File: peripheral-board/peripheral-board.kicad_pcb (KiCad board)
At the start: 2 copper layers, 165 x 100 mm, 145 parts, among them CON1001 AVR-ISP-10, IC1001 ATTINY48-A, P1001 Peripheral Bus, P1002 Power, SW2001 1, SW2002 2, SW2003 3, SW2004 4, SW2005 5, SW2006 6, SW2007 7, SW2008 8, SW2009 9, SW2010 0, SW2011 +, SW2012 ´, SW2013 BKSP, SW2014 TROLL, SW2015 §, SW2016 UP, SW2017 RMB, SW2018 Q, SW2019 W, SW2020 E, SW2021 R, SW2022 T, SW2023 Y, SW2024 U, SW2025 I, SW2026 O, SW2027 P, SW2028 Å, SW2029 ¨, SW2030 RETURN, SW2031 ALT_GR, SW2032 <, SW2033 LEFT, SW2034 MMB, SW2035 A, SW2036 S, SW2037 D, SW2038 F, SW2039 G, SW2040 H, SW2041 J, SW2042 K, SW2043 L, SW2044 Ö, SW2045 Ä, SW2046 ', SW2047 ESC, SW2048 TAB, SW2049 ALT, SW2050 DOWN, SW2051 LMB, SW2052 SHIFT_L, SW2053 Z, SW2054 X, SW2055 C, SW2056 V, SW2057 B, SW2058 N, SW2059 M, SW2060 ,, SW2061 ., SW2062 -, SW2063 SHIFT_R, SW2064 FN_R, SW2065 SPACE, SW2066 FN_L, SW2067 RIGHT, SW2068 CTRL, U2001 4017, U2002 4017, U2003 74HC00, U6001 TCA0372

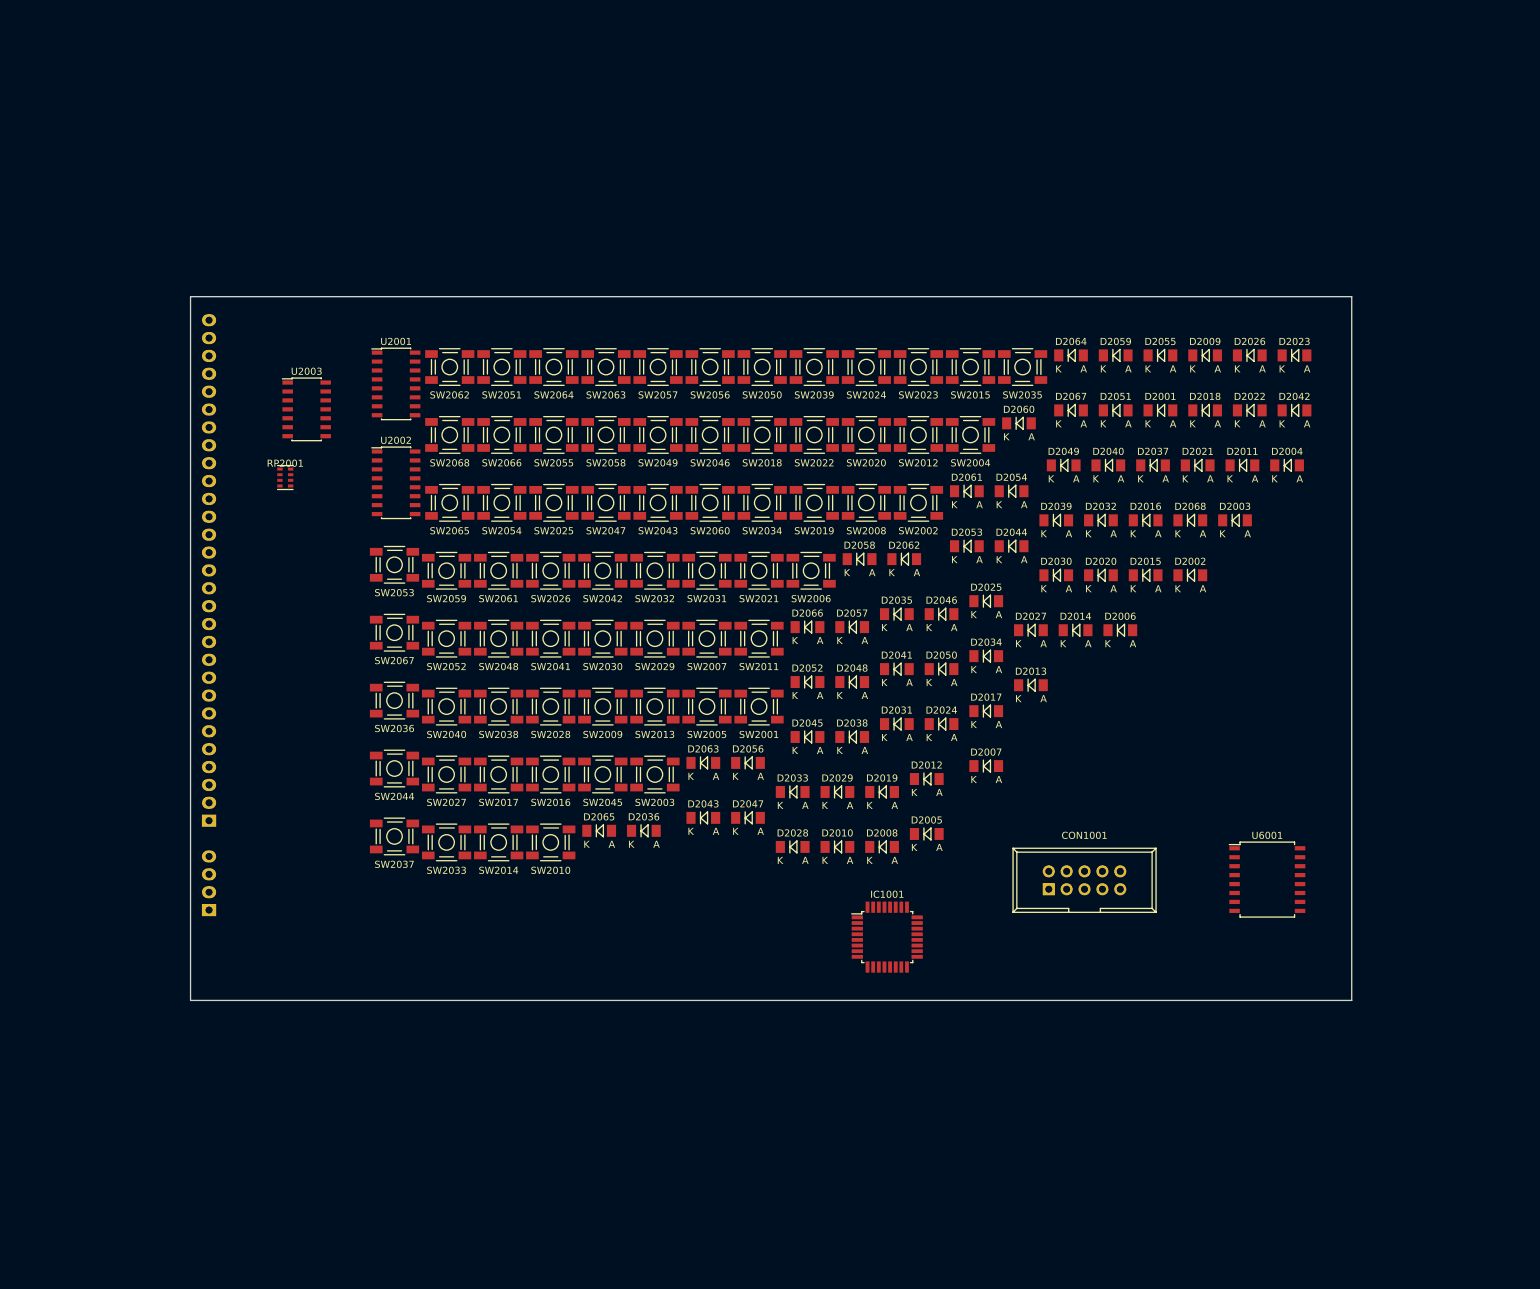
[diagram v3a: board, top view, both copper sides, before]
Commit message: keyboard switches and diodes placed
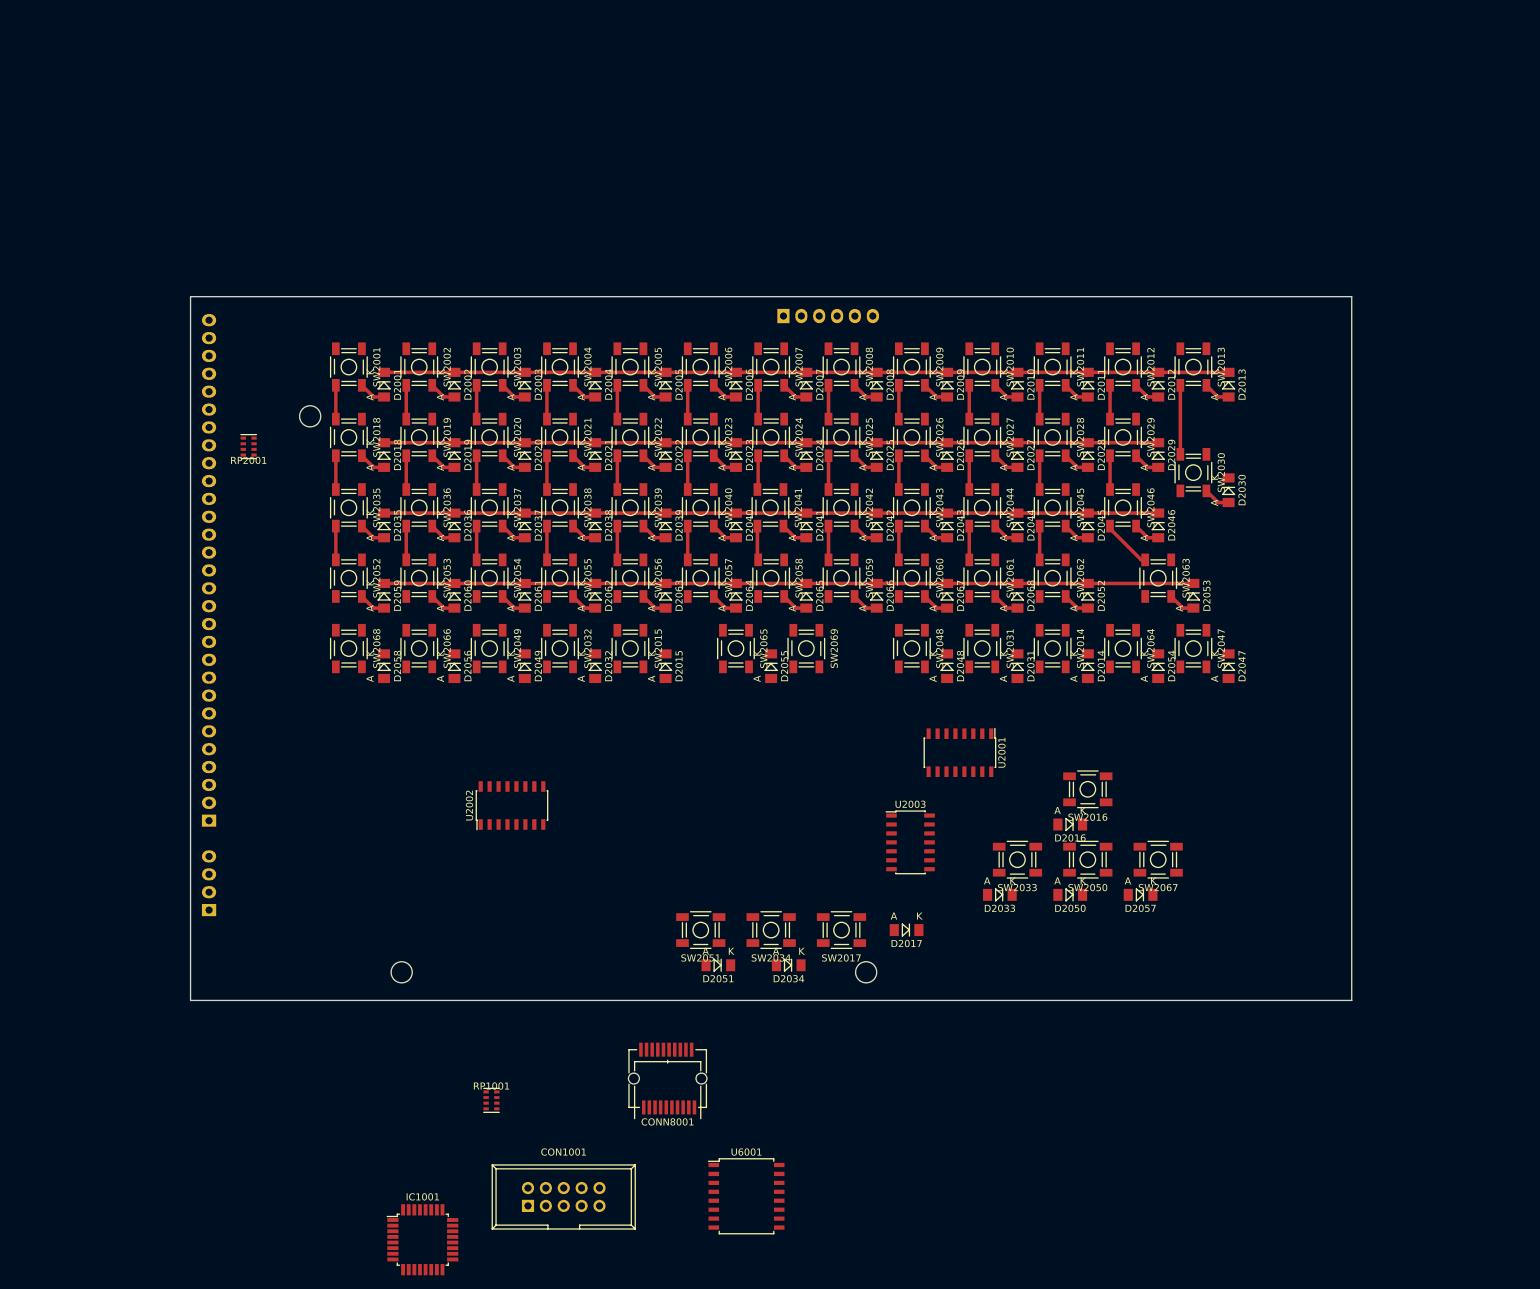
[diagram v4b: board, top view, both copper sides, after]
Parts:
- added CONN8001: 10056847-XY1LF, lib:10056847-XY1LF, F.Cu at (152.8, 161.1)
- added P9001: VGA, Socket_Strips:Socket_Strip_Straight_1x06, B.Cu at (169.2, 52.8)
- added REF**: 3mm, Mounting_Holes:MountingHole_3mm, F.Cu at (102.0, 67.0)
- added REF**: 3mm, Mounting_Holes:MountingHole_3mm, F.Cu at (181.0, 146.0)
- added REF**: 3mm, Mounting_Holes:MountingHole_3mm, F.Cu at (115.0, 146.0)
- added RP1001: 10k, Resistors_SMD:R_Cat16-4, F.Cu at (127.8, 164.2)
- added SW2069: SPACE, lib:SMD-TACT-5.2x5.2x2mm, F.Cu at (172.5, 100.0)
- moved D2018 116.8 mm to (112.5, 72.5), turned to 270 degrees
- moved SW2067 113.2 mm to (222.5, 130.0)
- moved D2001 110.4 mm to (112.5, 62.5), turned to 270 degrees
- moved D2059 109.4 mm to (112.5, 92.5), turned to 270 degrees
- moved D2002 108.0 mm to (122.5, 62.5), turned to 270 degrees
- moved U2003 105.6 mm to (187.3, 127.5)
- moved D2003 102.7 mm to (132.5, 62.5), turned to 270 degrees
- moved D2004 99.0 mm to (142.5, 62.5), turned to 270 degrees
- moved SW2035 97.8 mm to (107.5, 80.0), turned to 90 degrees
- moved D2051 97.0 mm to (160.0, 145.0), turned to 180 degrees
- moved U2001 95.7 mm to (194.3, 114.8), turned to 270 degrees
- moved SW2044 91.4 mm to (197.5, 80.0), turned to 90 degrees
- moved SW2010 91.2 mm to (197.5, 60.0), turned to 90 degrees
- moved SW2062 90.8 mm to (207.5, 90.0), turned to 90 degrees
- moved SW2013 90.5 mm to (227.5, 60.0), turned to 90 degrees
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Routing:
- net /Keyboard/Q0: track 0.00 -> 120.0 mm
- net /Keyboard/Q3: track 0.00 -> 115.0 mm
- net /Keyboard/Q2: track 0.00 -> 110.0 mm
- net /Keyboard/Q1: track 0.00 -> 110.0 mm
- net Net-(SW2012-Pad1): track 0.00 -> 16.8 mm
- net Net-(SW2007-Pad1): track 0.00 -> 14.5 mm
- net Net-(SW2011-Pad1): track 0.00 -> 14.4 mm
- net Net-(SW2010-Pad1): track 0.00 -> 14.4 mm
- net Net-(SW2009-Pad1): track 0.00 -> 14.4 mm
- net Net-(SW2008-Pad1): track 0.00 -> 14.4 mm
- net Net-(SW2006-Pad1): track 0.00 -> 14.4 mm
- net Net-(SW2005-Pad1): track 0.00 -> 14.4 mm
- net Net-(SW2004-Pad1): track 0.00 -> 14.4 mm
- net Net-(SW2003-Pad1): track 0.00 -> 14.4 mm
- net Net-(SW2002-Pad1): track 0.00 -> 14.4 mm
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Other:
- net class Default: clearance 0.2 -> 0.25; trace_width 0.25 -> 0.5; via_dia 0.8 -> 1; via_drill 0.4 -> 0.6
- rule trace_clearance: 0.2 -> 0.25
- rule via_min_drill: 0.3 -> 0.6
- rule via_min_size: 0.4 -> 1

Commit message: routed keyboard
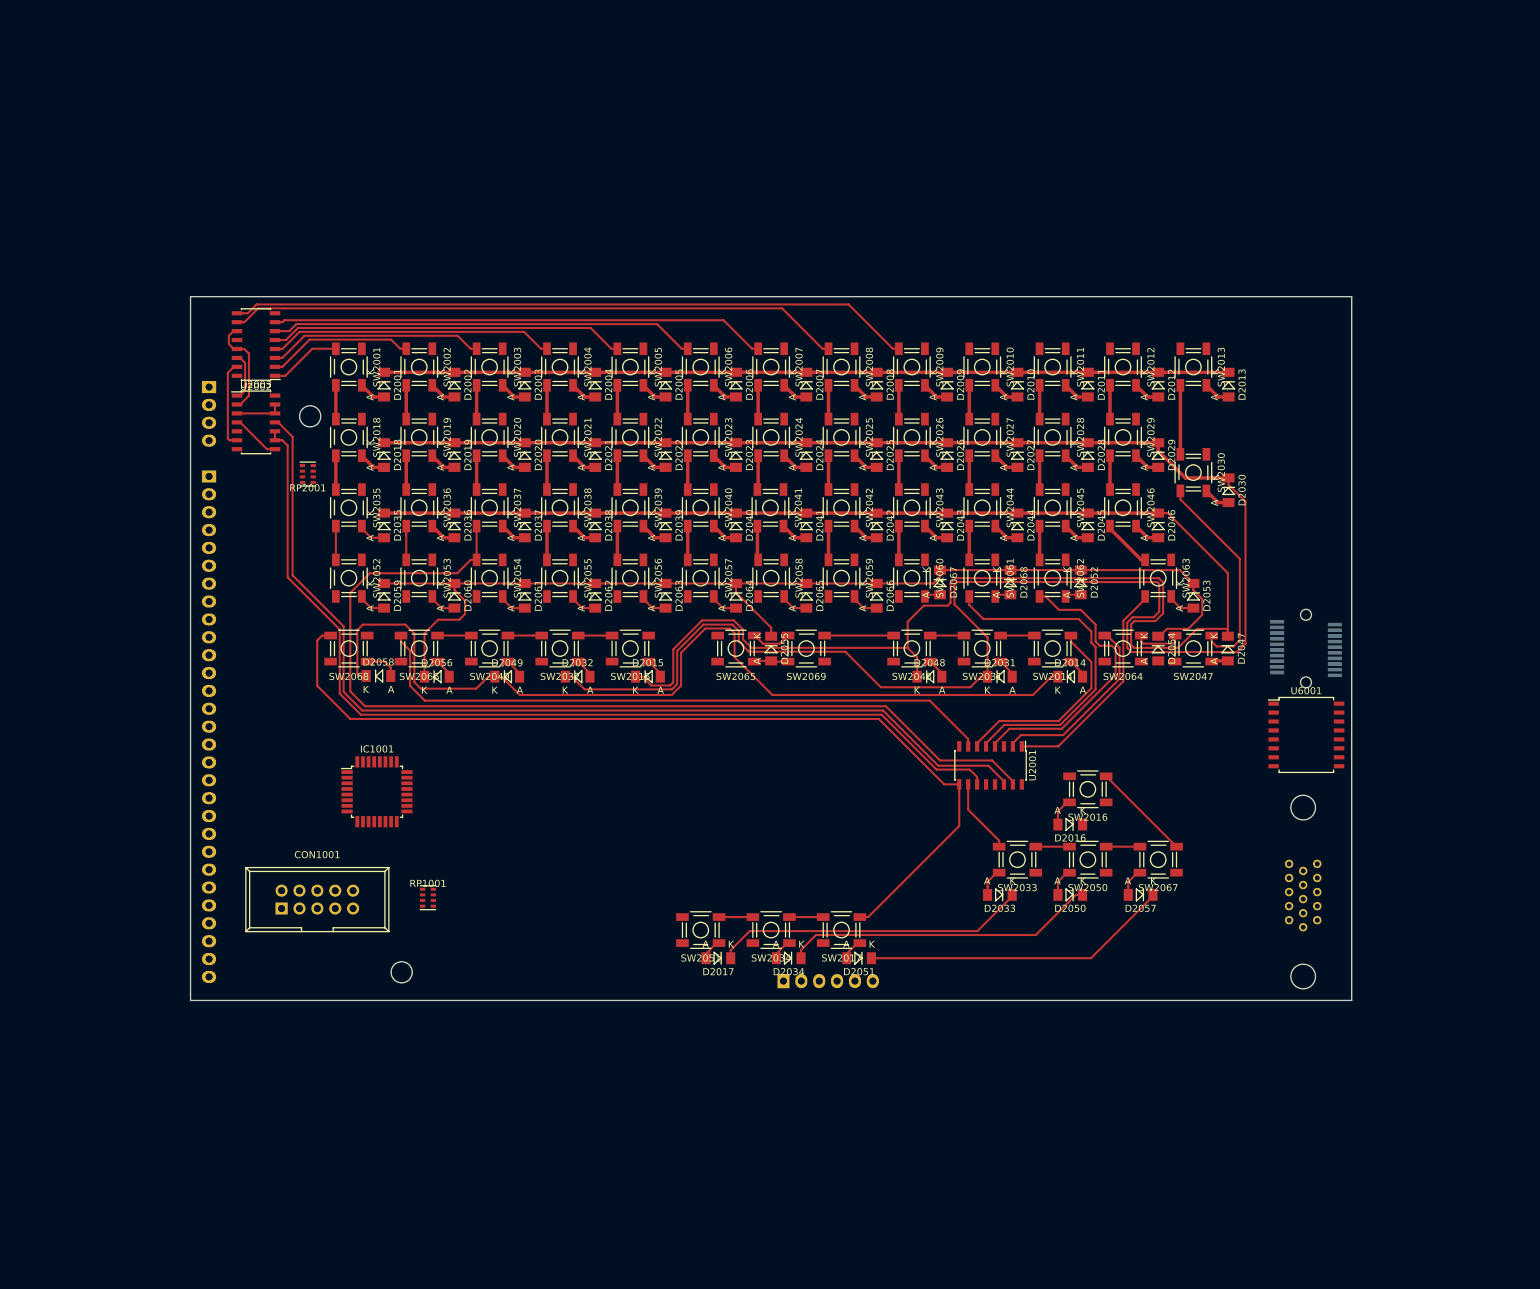
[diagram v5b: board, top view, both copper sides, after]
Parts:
- removed the REF** at (181.0, 146.0)
- added P9002: VGA DSUB, lib:HDDSUB-15-VGA, B.Cu at (243.1, 134.6)
- CONN8001: moved to B.Cu
- moved U2003 110.5 mm to (94.3, 67.9)
- moved CONN8001 109.4 mm to (243.5, 100.0), turned to 270 degrees
- moved U6001 103.1 mm to (243.6, 112.3)
- moved P9001 94.5 mm to (169.2, 147.2)
- moved U2002 74.9 mm to (94.3, 56.8), turned to 180 degrees
- moved P1002 74.3 mm to (87.6, 62.8), turned to 270 degrees
- moved IC1001 64.0 mm to (111.5, 120.3)
- moved CON1001 54.9 mm to (97.9, 136.9)
- moved P1001 48.9 mm to (87.6, 75.5), turned to 270 degrees
- moved RP1001 30.2 mm to (118.7, 135.4)
- moved D2017 27.0 mm to (160.0, 144.0)
- moved D2051 20.0 mm to (180.0, 144.0)
- moved RP2001 9.26 mm to (101.7, 75.2)
- moved U2001 4.71 mm to (198.7, 116.6)
- moved D2014 2.92 mm to (210.0, 104.0), turned to 0 degrees
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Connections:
- net Net-(SW2002-Pad1) renamed /Keyboard/COL1
- net Net-(SW2009-Pad1) renamed /Keyboard/COL8
- net Net-(SW2011-Pad1) renamed /Keyboard/COL10
- net Net-(SW2017-Pad1) renamed /Keyboard/COL16
- D2015 pad 1: /Keyboard/Q0 -> /Keyboard/Q2
- D2017 pad 1: /Keyboard/Q0 -> /Keyboard/Q1
- D2034 pad 1: /Keyboard/Q1 -> /Keyboard/Q2
- D2049 pad 1: /Keyboard/Q2 -> /Keyboard/Q0
- D2051 pad 1: /Keyboard/Q2 -> /Keyboard/Q3
- D2058 pad 1: /Keyboard/Q3 -> /Keyboard/Q0
- SW2001 pad 1: Net-(SW2001-Pad1) -> /Keyboard/COL0
- SW2003 pad 1: Net-(SW2003-Pad1) -> /Keyboard/COL2
- SW2004 pad 1: Net-(SW2004-Pad1) -> /Keyboard/COL3
- SW2005 pad 1: Net-(SW2005-Pad1) -> /Keyboard/COL4
- SW2006 pad 1: Net-(SW2006-Pad1) -> /Keyboard/COL5
- SW2007 pad 1: Net-(SW2007-Pad1) -> /Keyboard/COL6
- SW2008 pad 1: Net-(SW2008-Pad1) -> /Keyboard/COL7
- SW2010 pad 1: Net-(SW2010-Pad1) -> /Keyboard/COL9
- SW2012 pad 1: Net-(SW2012-Pad1) -> /Keyboard/COL11
- SW2013 pad 1: Net-(SW2013-Pad1) -> /Keyboard/COL12
- SW2014 pad 1: Net-(SW2014-Pad1) -> /Keyboard/COL13
- SW2015 pad 1: Net-(SW2015-Pad1) -> /Keyboard/COL14
- SW2016 pad 1: Net-(SW2016-Pad1) -> /Keyboard/COL15
- SW2017 pad 2: Net-(D2017-Pad2) -> Net-(D2051-Pad2)
- SW2018 pad 1: Net-(SW2001-Pad1) -> /Keyboard/COL0
- SW2020 pad 1: Net-(SW2003-Pad1) -> /Keyboard/COL2
- SW2021 pad 1: Net-(SW2004-Pad1) -> /Keyboard/COL3
- SW2022 pad 1: Net-(SW2005-Pad1) -> /Keyboard/COL4
- SW2023 pad 1: Net-(SW2006-Pad1) -> /Keyboard/COL5
- SW2024 pad 1: Net-(SW2007-Pad1) -> /Keyboard/COL6
- SW2025 pad 1: Net-(SW2008-Pad1) -> /Keyboard/COL7
- SW2027 pad 1: Net-(SW2010-Pad1) -> /Keyboard/COL9
- SW2029 pad 1: Net-(SW2012-Pad1) -> /Keyboard/COL11
- SW2030 pad 1: Net-(SW2013-Pad1) -> /Keyboard/COL12
- SW2031 pad 1: Net-(SW2014-Pad1) -> /Keyboard/COL13
- SW2032 pad 1: Net-(SW2015-Pad1) -> /Keyboard/COL14
- SW2033 pad 1: Net-(SW2016-Pad1) -> /Keyboard/COL15
- SW2035 pad 1: Net-(SW2001-Pad1) -> /Keyboard/COL0
- SW2037 pad 1: Net-(SW2003-Pad1) -> /Keyboard/COL2
- SW2038 pad 1: Net-(SW2004-Pad1) -> /Keyboard/COL3
- SW2039 pad 1: Net-(SW2005-Pad1) -> /Keyboard/COL4
- SW2040 pad 1: Net-(SW2006-Pad1) -> /Keyboard/COL5
- SW2041 pad 1: Net-(SW2007-Pad1) -> /Keyboard/COL6
- SW2042 pad 1: Net-(SW2008-Pad1) -> /Keyboard/COL7
- SW2044 pad 1: Net-(SW2010-Pad1) -> /Keyboard/COL9
- SW2046 pad 1: Net-(SW2012-Pad1) -> /Keyboard/COL11
- SW2047 pad 1: Net-(SW2013-Pad1) -> /Keyboard/COL12
- SW2048 pad 1: Net-(SW2014-Pad1) -> /Keyboard/COL13
- SW2049 pad 1: Net-(SW2015-Pad1) -> /Keyboard/COL14
- SW2050 pad 1: Net-(SW2016-Pad1) -> /Keyboard/COL15
- SW2051 pad 2: Net-(D2051-Pad2) -> Net-(D2017-Pad2)
- SW2052 pad 1: Net-(SW2001-Pad1) -> /Keyboard/COL0
- SW2054 pad 1: Net-(SW2003-Pad1) -> /Keyboard/COL2
- SW2055 pad 1: Net-(SW2004-Pad1) -> /Keyboard/COL3
- SW2056 pad 1: Net-(SW2005-Pad1) -> /Keyboard/COL4
- SW2057 pad 1: Net-(SW2006-Pad1) -> /Keyboard/COL5
- SW2058 pad 1: Net-(SW2007-Pad1) -> /Keyboard/COL6
- SW2059 pad 1: Net-(SW2008-Pad1) -> /Keyboard/COL7
- SW2061 pad 1: Net-(SW2010-Pad1) -> /Keyboard/COL9
- SW2063 pad 1: Net-(SW2012-Pad1) -> /Keyboard/COL11
- SW2064 pad 1: Net-(SW2013-Pad1) -> /Keyboard/COL12
- SW2065 pad 1: Net-(SW2014-Pad1) -> /Keyboard/COL13
- SW2066 pad 1: Net-(SW2015-Pad1) -> /Keyboard/COL14
- SW2067 pad 1: Net-(SW2016-Pad1) -> /Keyboard/COL15
- SW2069 pad 1: Net-(SW2014-Pad1) -> /Keyboard/COL13
- U2001 pad 1: Net-(SW2014-Pad1) -> /Keyboard/COL11
- U2001 pad 10: Net-(SW2013-Pad1) -> /Keyboard/COL15
- U2001 pad 15: Net-(SW2001-Pad1) -> /Keyboard/COL2
- U2001 pad 2: Net-(SW2010-Pad1) -> /Keyboard/COL12
- U2001 pad 5: Net-(SW2015-Pad1) -> /Keyboard/COL9
- U2001 pad 6: Net-(SW2016-Pad1) -> /Keyboard/COL13
- U2001 pad 7: Net-(SW2012-Pad1) -> /Keyboard/COL14
- U2002 pad 1: Net-(SW2006-Pad1) -> /Keyboard/COL0
- U2002 pad 10: Net-(SW2005-Pad1) -> /Keyboard/COL7
- U2002 pad 3: Net-(SW2001-Pad1) -> /Keyboard/COL2
- U2002 pad 4: Net-(SW2003-Pad1) -> /Keyboard/COL3
- U2002 pad 5: Net-(SW2007-Pad1) -> /Keyboard/COL4
- U2002 pad 6: Net-(SW2008-Pad1) -> /Keyboard/COL5
- U2002 pad 7: Net-(SW2004-Pad1) -> /Keyboard/COL6
- U2003 pad 1: Net-(U2001-Pad11) -> /Keyboard/CLK
- U2003 pad 10: /Keyboard/~RESET -> Net-(U2001-Pad11)
- U2003 pad 11: Net-(U2003-Pad11) -> Net-(U2001-Pad14)
- U2003 pad 12: /Keyboard/CLK -> Net-(U2003-Pad12)
- U2003 pad 13: Net-(U2002-Pad11) -> Net-(U2003-Pad12)
- U2003 pad 14: VCC -> +3V3
- U2003 pad 2: Net-(U2001-Pad11) -> Net-(U2002-Pad11)
- U2003 pad 3: Net-(U2003-Pad3) -> Net-(U2003-Pad12)
- U2003 pad 4: Net-(U2003-Pad11) -> Net-(U2003-Pad4)
- U2003 pad 5: Net-(U2003-Pad11) -> /Keyboard/~RESET
- U2003 pad 6: Net-(U2001-Pad14) -> Net-(U2002-Pad15)
- U2003 pad 8: Net-(U2002-Pad15) -> Net-(U2003-Pad4)
- U2003 pad 9: Net-(U2003-Pad3) -> Net-(U2001-Pad11)
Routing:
- net /Keyboard/Q1: track 110.0 -> 339.0 mm
- net /Keyboard/Q2: track 110.0 -> 302.9 mm
- net /Keyboard/COL2: track 0.00 -> 178.9 mm
- net Net-(U2001-Pad14): track 0.00 -> 142.1 mm
- net /Keyboard/COL16: track 0.00 -> 140.7 mm
- net Net-(U2001-Pad11): track 0.00 -> 138.2 mm
- net /Keyboard/Q0: track 120.0 -> 250.7 mm
- net /Keyboard/COL14: track 0.00 -> 105.6 mm
- net /Keyboard/COL7: track 0.00 -> 101.6 mm
- net /Keyboard/COL8: track 14.4 -> 111.6 mm
- net /Keyboard/Q3: track 115.0 -> 201.1 mm
- net /Keyboard/COL6: track 0.00 -> 84.9 mm
- net /Keyboard/COL5: track 0.00 -> 74.9 mm
- net /Keyboard/COL12: track 0.00 -> 73.7 mm
- net /Keyboard/COL4: track 0.00 -> 65.0 mm
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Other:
- net class Default: trace_width 0.5 -> 0.3
- board text added: "Battery"
- board text added: "DC IN"
- board text added: "SMPS"
